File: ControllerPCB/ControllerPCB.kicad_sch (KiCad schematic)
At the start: 45 parts, among them J1 2x4 Pickup Conn, J10 Conn_01x03_Pin, J11 Conn_01x03_Pin, J12 Conn_01x03_Pin, J2 Conn_01x03_Pin, J3 USB_B_Micro, J4 10-pin SWD Connector, J5 1x4 String Output Conn, J6 2x20 Conn_1, J7 2x20 Conn_2, J8 Conn_01x03_Pin, J9 Conn_01x03_Pin, SW1 SW_SPDT, U2 STM32F439ZIT6, Y2 WE-XTAL_CFPX-218

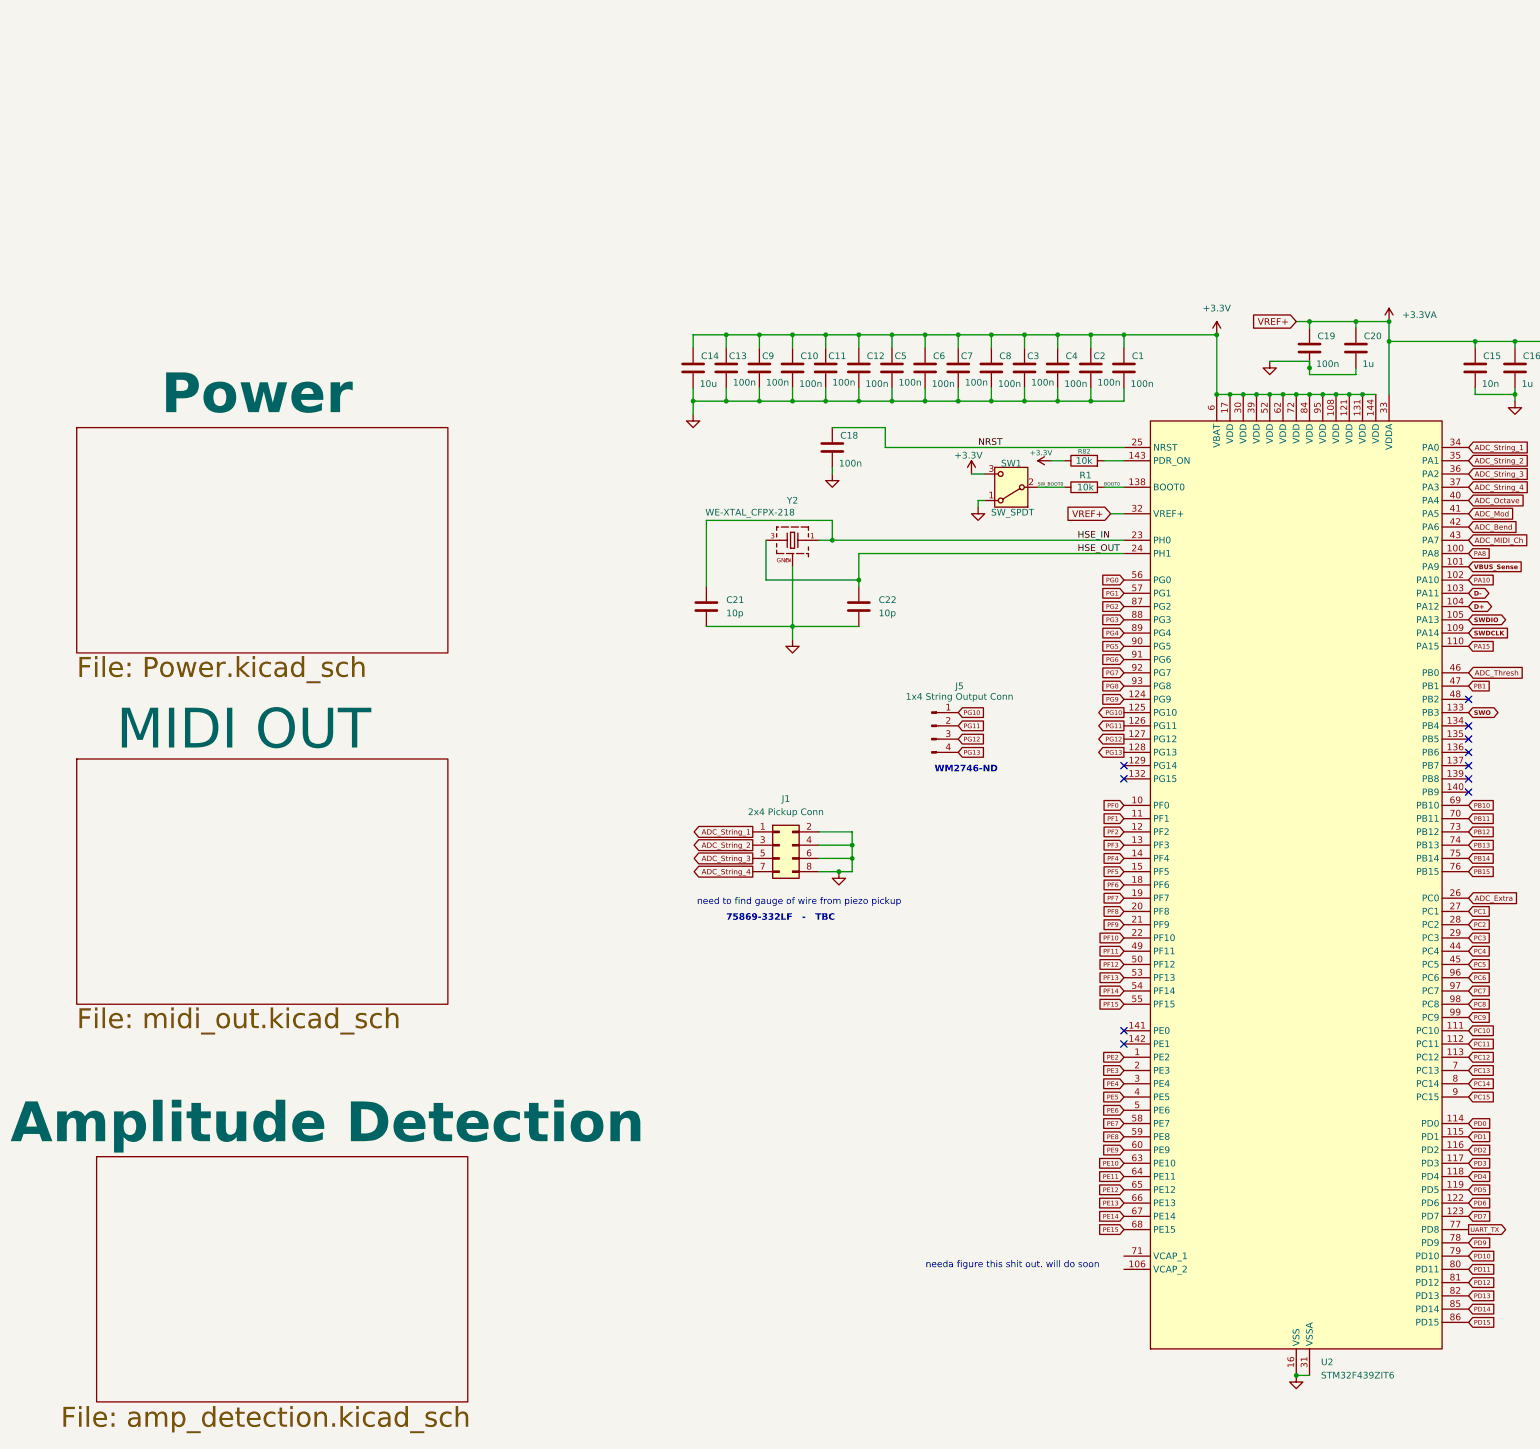
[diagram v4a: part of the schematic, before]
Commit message: Added VCAP 1/2 capacitors. These assist the internal voltage regulator. We don't have an option to turn the regulator off so it is always on.
Swapped the crystal oscillator out for a different one.

Tweaked the VREF+ scheme a bit - changed the 100nF decoupling cap to 10nF to comply with the datasheet when VREF+ is connected to VDDA
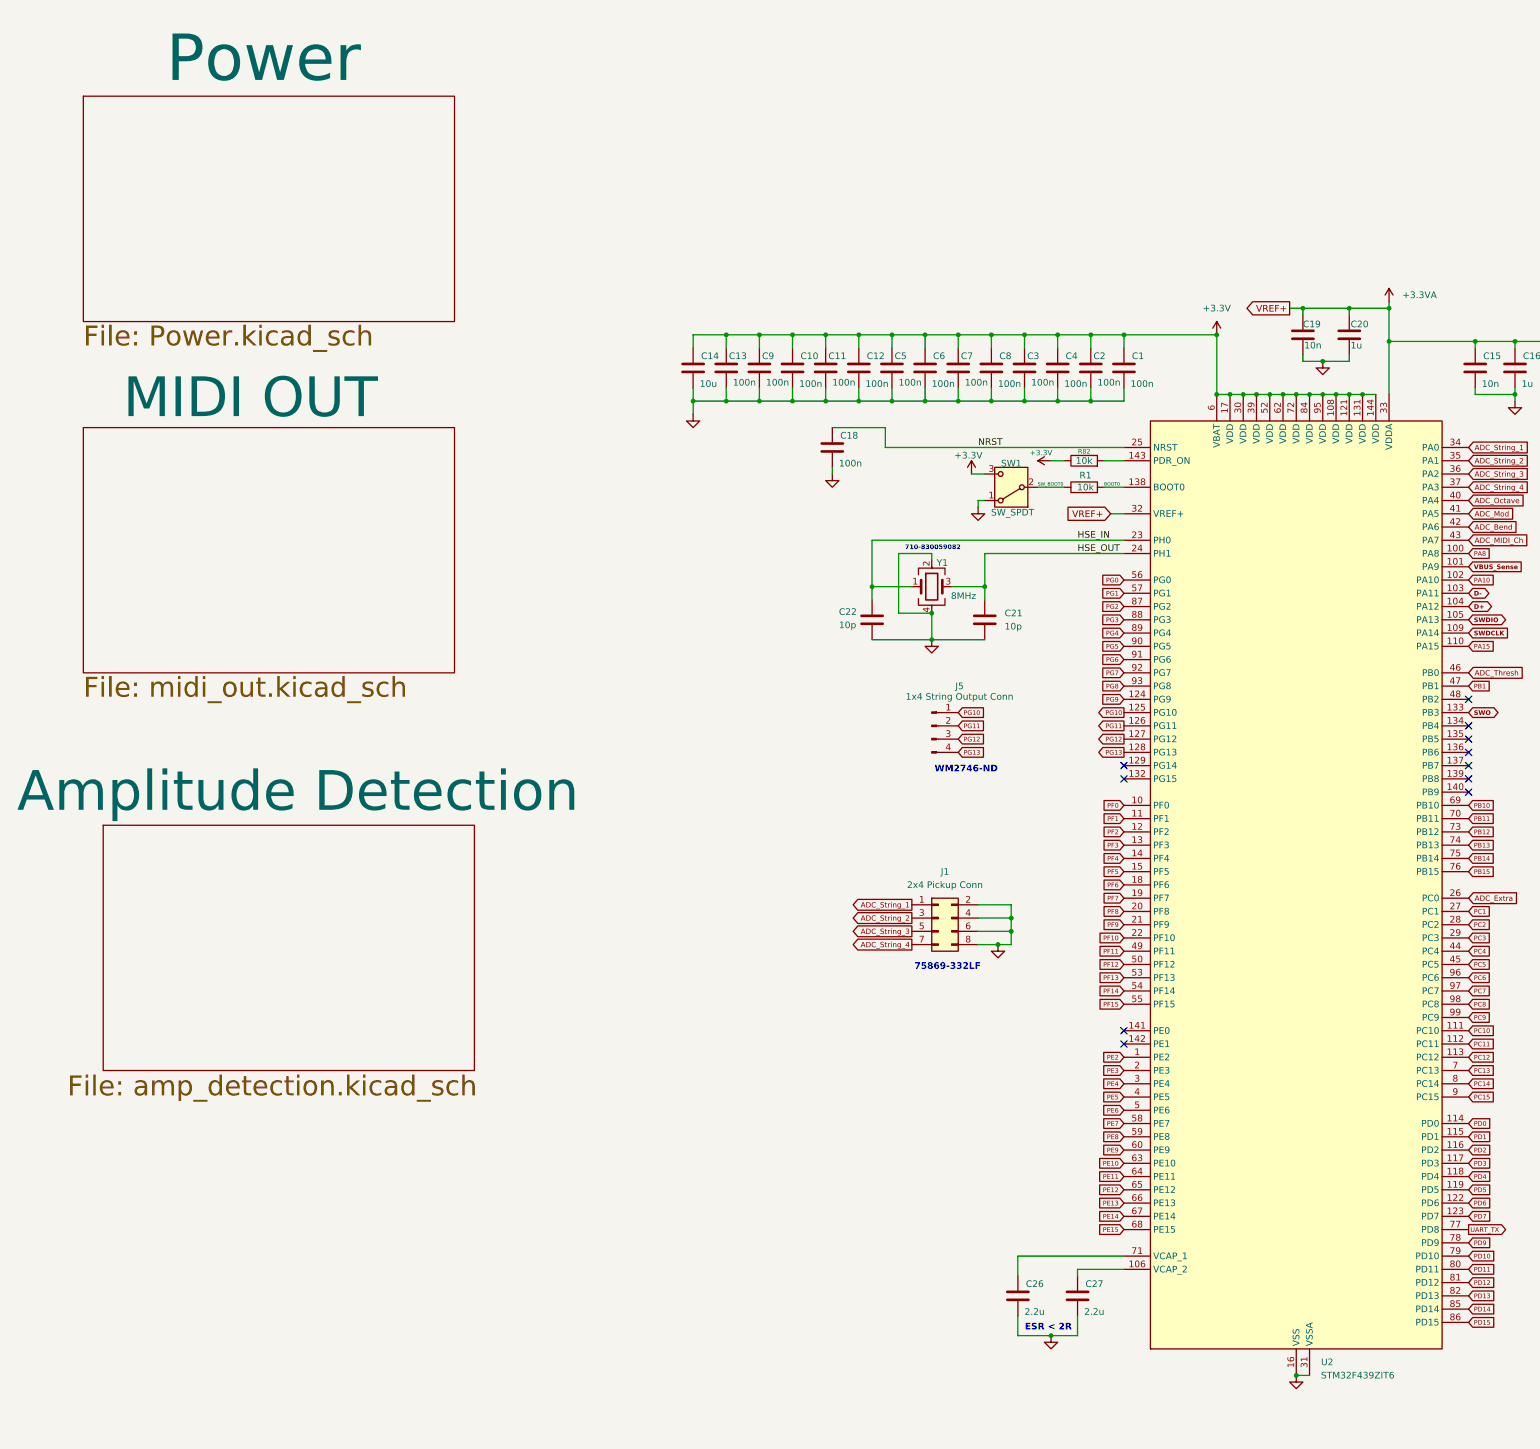
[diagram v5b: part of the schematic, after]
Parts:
- removed Y2: WE-XTAL_CFPX-218, crysoscill:WE-SPXO_IQXO-791, symbol Crystal_Oscillator_CFPX_218:WE-XTAL_CFPX-218
- added C26, C27: 2.2u, Capacitor_SMD:C_01005_0402Metric, symbol Device:C
- added Y1: 8MHz, symbol Device:Crystal_GND24
- C19: value 100n -> 10n
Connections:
- net GND: now also C26.2, C27.2, Y1.2, Y1.4
- net HSE_IN: now also C22.1, Y1.1; no longer C21.1
- net HSE_OUT: now also C21.1, Y1.3; no longer C22.1
- net at U2.106 (VCAP_2): now also C27.1
- net at U2.71 (VCAP_1): now also C26.1
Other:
- note added: "710-830059082"
- note added: "75869-332LF"
- note added: "ESR < 2R"
- note removed: "75869-332LF - TBC"
- note removed: "need to find gauge of wire from piezo pickup"
- note removed: "needa figure this shit out. will do soon"
- moved on the sheet: C20, C21, C22, J1

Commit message: Organized the schematic a bit
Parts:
- C14, C15: footprint Capacitor_SMD:C_01005_0402Metric -> Capacitor_SMD:C_0603_1608Metric
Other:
- note added: "2x40 Neck PCB Input Pins"
- note added: "Exterior MIDI Control Inputs"
- note added: "LMK107BJ225MAHT"
- note added: "Piezo Pickup Input"
- note added: "SWD Debug"
- note added: "String Output"
- note added: "USB Micro B"
- note removed: "Many GND and +3.3V here since each ADC MIDI control input voltage is varied using a 100kOhm potentiometer"
- moved on the sheet: C1, C10, C11, C12, C13, C14, C15, C16, C17, C18, C19, C2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

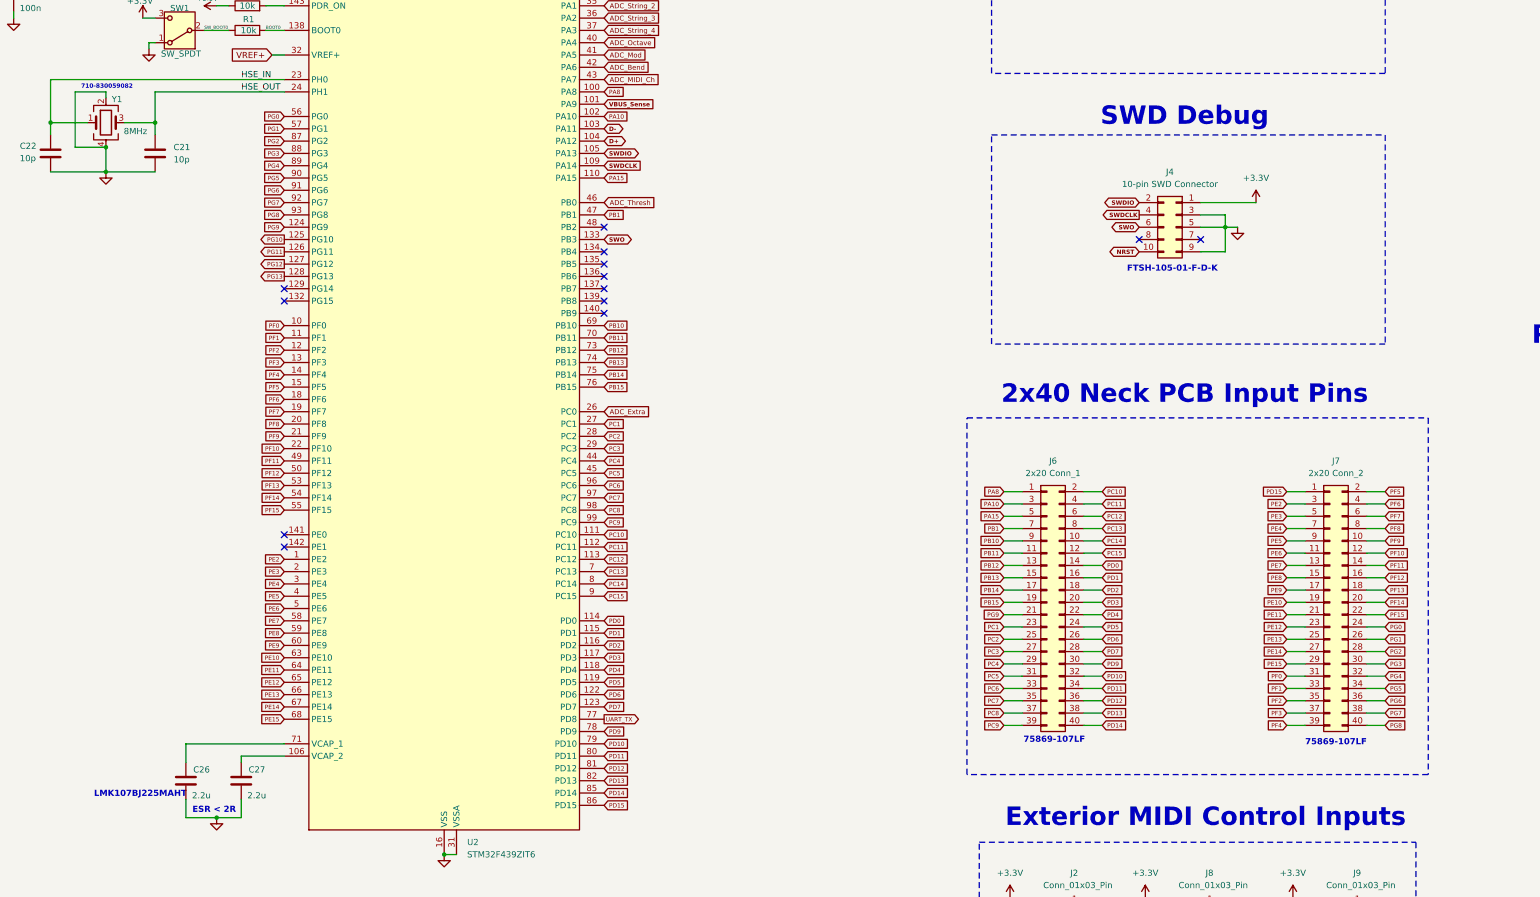
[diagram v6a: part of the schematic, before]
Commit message: Created a stm32cubeide project with the exact pinout of the controller schematic. Double checked the pinouts and renamed the 80 inputs to be input_# for readability
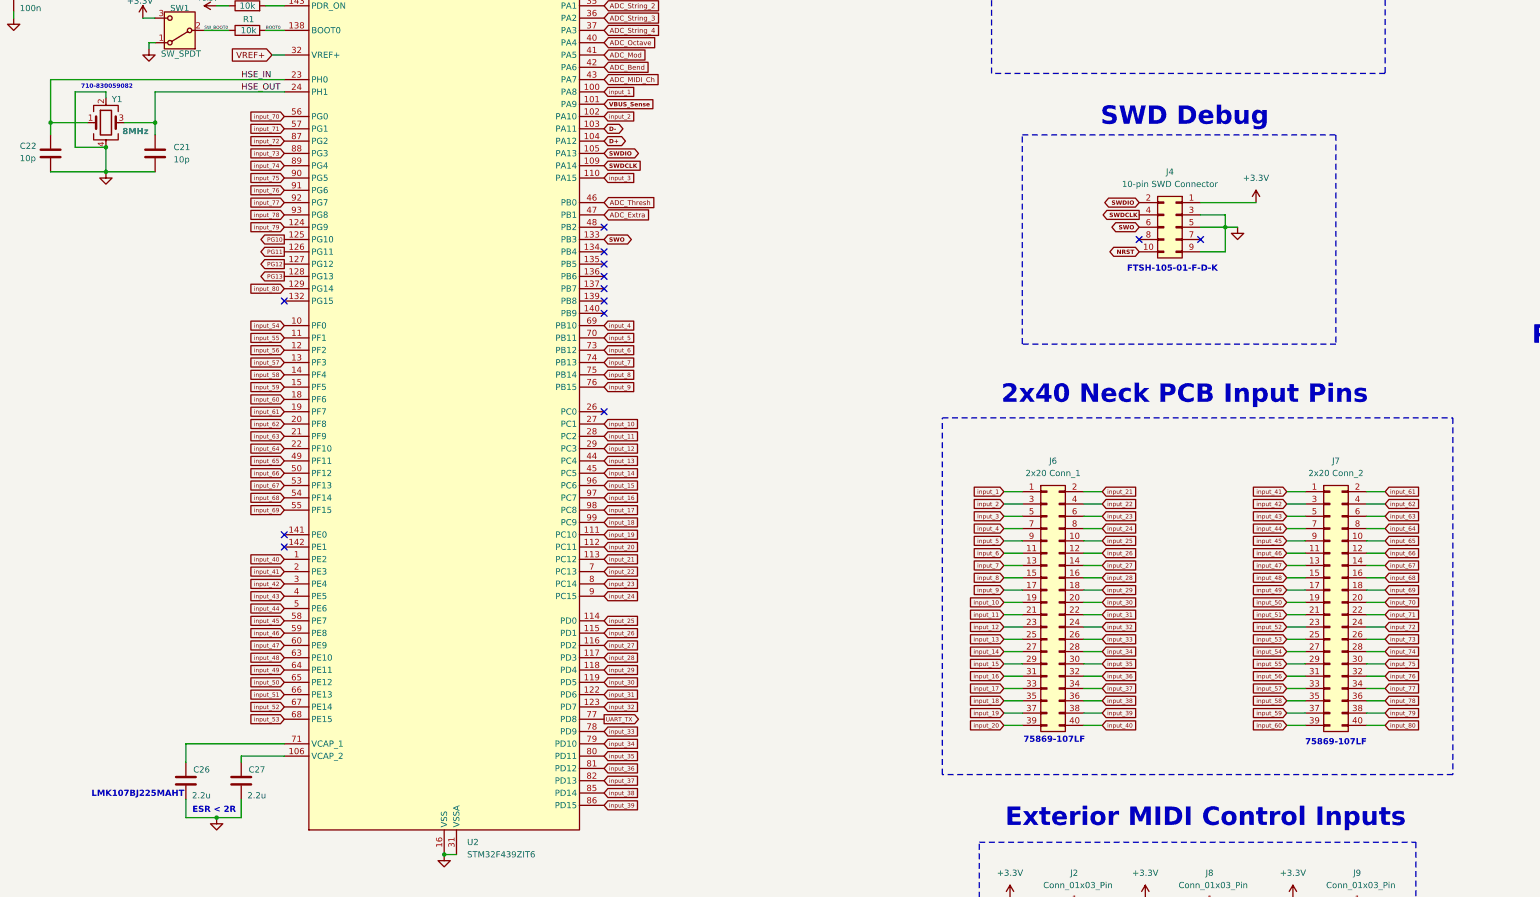
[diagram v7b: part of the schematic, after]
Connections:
- net ADC_Extra: now also U2.47 (PB1); no longer U2.26 (PC0)
- net input_80: now reaches U2.129 (PG14)
- net input_80: now also J7.40 (Pin_40)
- net PA10 renamed input_2
- net PA15 renamed input_3
- net PA8 renamed input_1
- net PB1 renamed input_4
- net input_4: now also U2.69 (PB10); no longer U2.47 (PB1)
- net PB10 renamed input_5
- net input_5: now also U2.70 (PB11); no longer U2.69 (PB10)
- net PB11 renamed input_6
- net input_6: now also U2.73 (PB12); no longer U2.70 (PB11)
- net PB12 renamed input_7
- net input_7: now also U2.74 (PB13); no longer U2.73 (PB12)
- net PB13 renamed input_8
- net input_8: now also U2.75 (PB14); no longer U2.74 (PB13)
- net PB14 renamed input_9
- net input_9: now also U2.76 (PB15); no longer U2.75 (PB14)
- net PB15 renamed input_10
- net input_10: now also U2.27 (PC1); no longer U2.76 (PB15)
- net PC1 renamed input_12
- net input_12: now also U2.29 (PC3); no longer U2.27 (PC1)
- net PC10 renamed input_19
- net input_19: now also J6.37 (Pin_37); no longer J6.2 (Pin_2)
- net PC11 renamed input_20
- net input_20: now also J6.39 (Pin_39); no longer J6.4 (Pin_4)
- net PC12 renamed input_21
- net input_21: now also J6.2 (Pin_2); no longer J6.6 (Pin_6)
- net PC13 renamed input_22
- net input_22: now also J6.4 (Pin_4); no longer J6.8 (Pin_8)
- net PC14 renamed input_23
- net input_23: now also J6.6 (Pin_6); no longer J6.10 (Pin_10)
- net PC15 renamed input_24
- net input_24: now also J6.8 (Pin_8); no longer J6.12 (Pin_12)
- net PC2 renamed input_11
- net input_11: now also J6.21 (Pin_21); no longer J6.25 (Pin_25)
- net PC3 renamed input_14
- net input_14: now also U2.45 (PC5); no longer U2.29 (PC3)
- net PC4 renamed input_13
- net input_13: now also J6.25 (Pin_25); no longer J6.29 (Pin_29)
- net PC5 renamed input_16
- net input_16: now also U2.97 (PC7); no longer U2.45 (PC5)
- net PC6 renamed input_15
- net input_15: now also J6.29 (Pin_29); no longer J6.33 (Pin_33)
- net PC7 renamed input_18
- net input_18: now also U2.99 (PC9); no longer U2.97 (PC7)
- net PC8 renamed input_17
- net input_17: now also J6.33 (Pin_33); no longer J6.37 (Pin_37)
- removed net PC9: J6.39 (Pin_39), U2.99 (PC9)
- net PD0 renamed input_25
- net input_25: now also J6.10 (Pin_10); no longer J6.14 (Pin_14)
- net PD1 renamed input_26
- net input_26: now also J6.12 (Pin_12); no longer J6.16 (Pin_16)
- net PD10 renamed input_34
- net input_34: now also J6.28 (Pin_28); no longer J6.32 (Pin_32)
- net PD11 renamed input_35
- net input_35: now also J6.30 (Pin_30); no longer J6.34 (Pin_34)
- net PD12 renamed input_36
- net input_36: now also J6.32 (Pin_32); no longer J6.36 (Pin_36)
- net PD13 renamed input_37
- net input_37: now also J6.34 (Pin_34); no longer J6.38 (Pin_38)
- net PD14 renamed input_38
- net input_38: now also J6.36 (Pin_36); no longer J6.40 (Pin_40)
- net PD15 renamed input_39
- net input_39: now also J6.38 (Pin_38); no longer J7.1 (Pin_1)
- net PD2 renamed input_27
- net input_27: now also J6.14 (Pin_14); no longer J6.18 (Pin_18)
- net PD3 renamed input_28
- net input_28: now also J6.16 (Pin_16); no longer J6.20 (Pin_20)
- net PD4 renamed input_29
- net input_29: now also J6.18 (Pin_18); no longer J6.22 (Pin_22)
- net PD5 renamed input_30
- net input_30: now also J6.20 (Pin_20); no longer J6.24 (Pin_24)
- net PD6 renamed input_31
- net input_31: now also J6.22 (Pin_22); no longer J6.26 (Pin_26)
- net PD7 renamed input_32
- net input_32: now also J6.24 (Pin_24); no longer J6.28 (Pin_28)
- net PD9 renamed input_33
- net input_33: now also J6.26 (Pin_26); no longer J6.30 (Pin_30)
- net PE10 renamed input_48
- net input_48: now also J7.15 (Pin_15); no longer J7.19 (Pin_19)
- net PE11 renamed input_49
- net input_49: now also J7.17 (Pin_17); no longer J7.21 (Pin_21)
- net PE12 renamed input_50
- net input_50: now also J7.19 (Pin_19); no longer J7.23 (Pin_23)
- net PE13 renamed input_51
- net input_51: now also J7.21 (Pin_21); no longer J7.25 (Pin_25)
- net PE14 renamed input_52
- net input_52: now also J7.23 (Pin_23); no longer J7.27 (Pin_27)
- net PE15 renamed input_53
- net input_53: now also J7.25 (Pin_25); no longer J7.29 (Pin_29)
- net PE2 renamed input_40
- net input_40: now also J6.40 (Pin_40); no longer J7.3 (Pin_3)
- net PE3 renamed input_41
- net input_41: now also J7.1 (Pin_1); no longer J7.5 (Pin_5)
- net PE4 renamed input_42
- net input_42: now also J7.3 (Pin_3); no longer J7.7 (Pin_7)
- net PE5 renamed input_43
- net input_43: now also J7.5 (Pin_5); no longer J7.9 (Pin_9)
- net PE6 renamed input_44
- net input_44: now also J7.7 (Pin_7); no longer J7.11 (Pin_11)
- net PE7 renamed input_45
- net input_45: now also J7.9 (Pin_9); no longer J7.13 (Pin_13)
- net PE8 renamed input_46
- net input_46: now also J7.11 (Pin_11); no longer J7.15 (Pin_15)
- net PE9 renamed input_47
- net input_47: now also J7.13 (Pin_13); no longer J7.17 (Pin_17)
- net PF0 renamed input_54
- net input_54: now also J7.27 (Pin_27); no longer J7.31 (Pin_31)
- net PF1 renamed input_55
- net input_55: now also J7.29 (Pin_29); no longer J7.33 (Pin_33)
- net PF10 renamed input_64
- net input_64: now also J7.8 (Pin_8); no longer J7.12 (Pin_12)
- net PF11 renamed input_65
- net input_65: now also J7.10 (Pin_10); no longer J7.14 (Pin_14)
- net PF12 renamed input_66
- net input_66: now also J7.12 (Pin_12); no longer J7.16 (Pin_16)
- net PF13 renamed input_67
- net input_67: now also J7.14 (Pin_14); no longer J7.18 (Pin_18)
- net PF14 renamed input_68
- net input_68: now also J7.16 (Pin_16); no longer J7.20 (Pin_20)
- net PF15 renamed input_69
- net input_69: now also J7.18 (Pin_18); no longer J7.22 (Pin_22)
- net PF2 renamed input_56
- net input_56: now also J7.31 (Pin_31); no longer J7.35 (Pin_35)
- net PF3 renamed input_57
- net input_57: now also J7.33 (Pin_33); no longer J7.37 (Pin_37)
- net PF4 renamed input_58
- net input_58: now also J7.35 (Pin_35); no longer J7.39 (Pin_39)
- net PF5 renamed input_59
- net input_59: now also J7.37 (Pin_37); no longer J7.2 (Pin_2)
- net PF6 renamed input_60
- net input_60: now also J7.39 (Pin_39); no longer J7.4 (Pin_4)
- net PF7 renamed input_61
- net input_61: now also J7.2 (Pin_2); no longer J7.6 (Pin_6)
- net PF8 renamed input_62
- net input_62: now also J7.4 (Pin_4); no longer J7.8 (Pin_8)
- net PF9 renamed input_63
- net input_63: now also J7.6 (Pin_6); no longer J7.10 (Pin_10)
- net PG0 renamed input_70
- net input_70: now also J7.20 (Pin_20); no longer J7.24 (Pin_24)
- net PG1 renamed input_71
- net input_71: now also J7.22 (Pin_22); no longer J7.26 (Pin_26)
- net PG2 renamed input_72
- net input_72: now also J7.24 (Pin_24); no longer J7.28 (Pin_28)
- net PG3 renamed input_73
- net input_73: now also J7.26 (Pin_26); no longer J7.30 (Pin_30)
- net PG4 renamed input_74
- net input_74: now also J7.28 (Pin_28); no longer J7.32 (Pin_32)
- net PG5 renamed input_75
- net input_75: now also J7.30 (Pin_30); no longer J7.34 (Pin_34)
- net PG6 renamed input_76
- net input_76: now also J7.32 (Pin_32); no longer J7.36 (Pin_36)
- net PG7 renamed input_77
- net input_77: now also J7.34 (Pin_34); no longer J7.38 (Pin_38)
- net PG8 renamed input_78
- net input_78: now also J7.36 (Pin_36); no longer J7.40 (Pin_40)
- net PG9 renamed input_79
- net input_79: now also J7.38 (Pin_38); no longer J6.21 (Pin_21)
